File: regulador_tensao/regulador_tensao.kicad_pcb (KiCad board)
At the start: 2 copper layers, 25.4 x 13 mm, 6 parts, among them P1 CONN_IN_5V, P2 CONN_OUT_3V3, U1 SPX3819M5-L-3-3

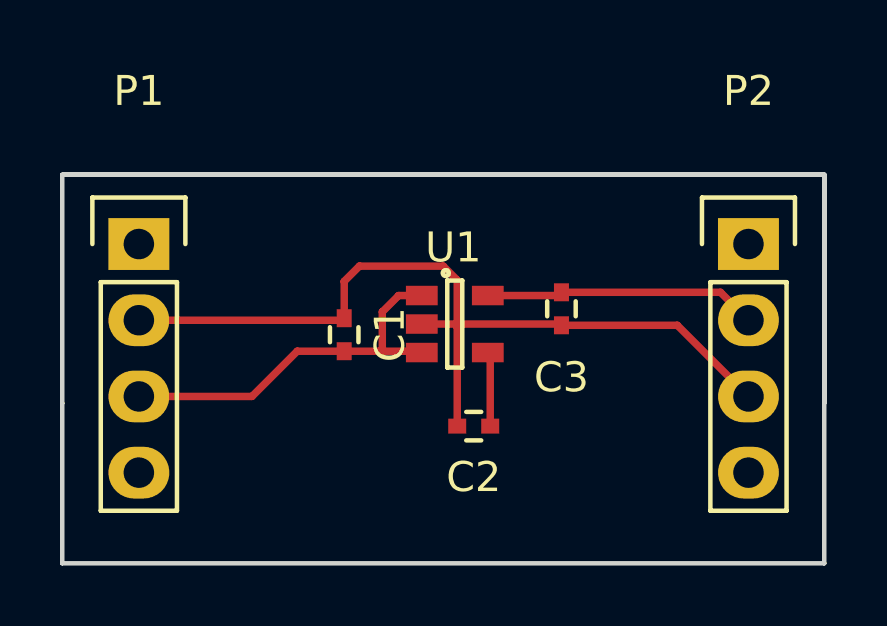
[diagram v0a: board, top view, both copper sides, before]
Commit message: Reg. tensao finished, with renderings. Minor fixes in usb-serial
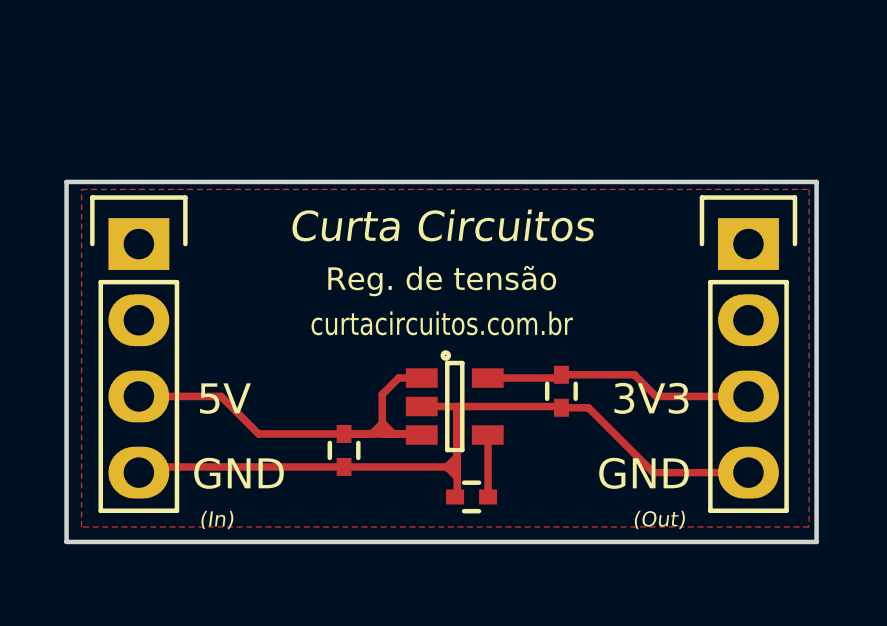
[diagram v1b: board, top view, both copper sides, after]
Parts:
- moved C1 3.86 mm to (159.0, 105.0), turned to 270 degrees
- moved C3 2.75 mm to (166.2, 103.0)
- moved U1 2.75 mm to (162.7, 103.5)
- moved C2 2.36 mm to (163.2, 106.5)
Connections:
- P1 pad 2: Earth -> Net-(P1-Pad2)
- P1 pad 4: Net-(P1-Pad4) -> Earth
- P2 pad 2: +3V3 -> Net-(P2-Pad2)
- P2 pad 3: Earth -> +3V3
- P2 pad 4: Net-(P2-Pad4) -> Earth
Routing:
- net +5V: track 12.9 -> 16.1 mm
- added copper zone on F.Cu, net Earth
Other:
- board size 25.4 x 13 mm -> 25 x 12 mm
- board text added: "(In)"
- board text added: "(Out)"
- board text added: "3V3"
- board text added: "5V"
- board text added: "Curta Circuitos"
- board text added: "GND"
- board text added: "Reg. de tensão"
- board text added: "curtacircuitos.com.br"
